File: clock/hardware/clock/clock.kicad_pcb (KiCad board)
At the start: 2 copper layers, 26 parts, among them J1 USB_B_Micro, J2 7SEG_DEBUG, J3 Conn_ARM_JTAG_SWD_10, U1 LM1117-3.3, U2 AS1115, U3 LTC-4727JS, U4 STM32L151C8TxA, Y1 32.768kHz

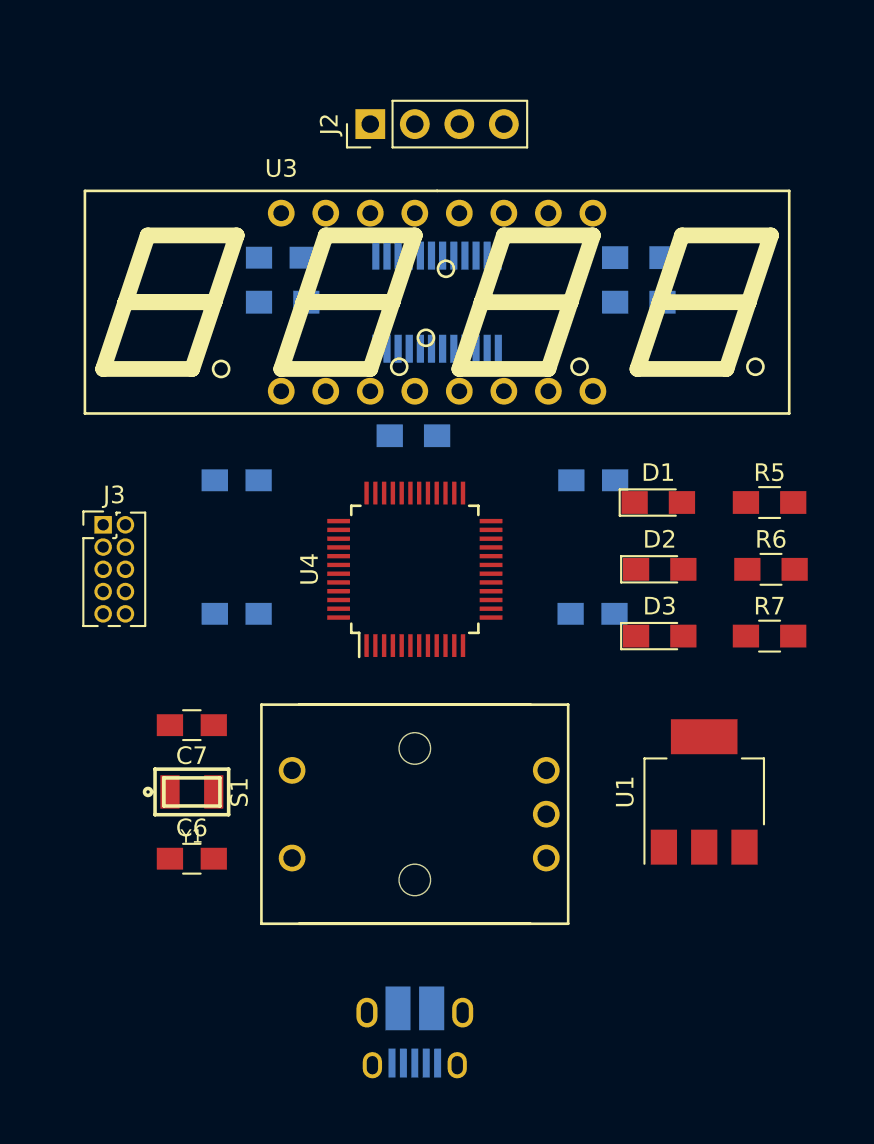
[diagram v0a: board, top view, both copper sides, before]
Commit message: Add clock edge cuts
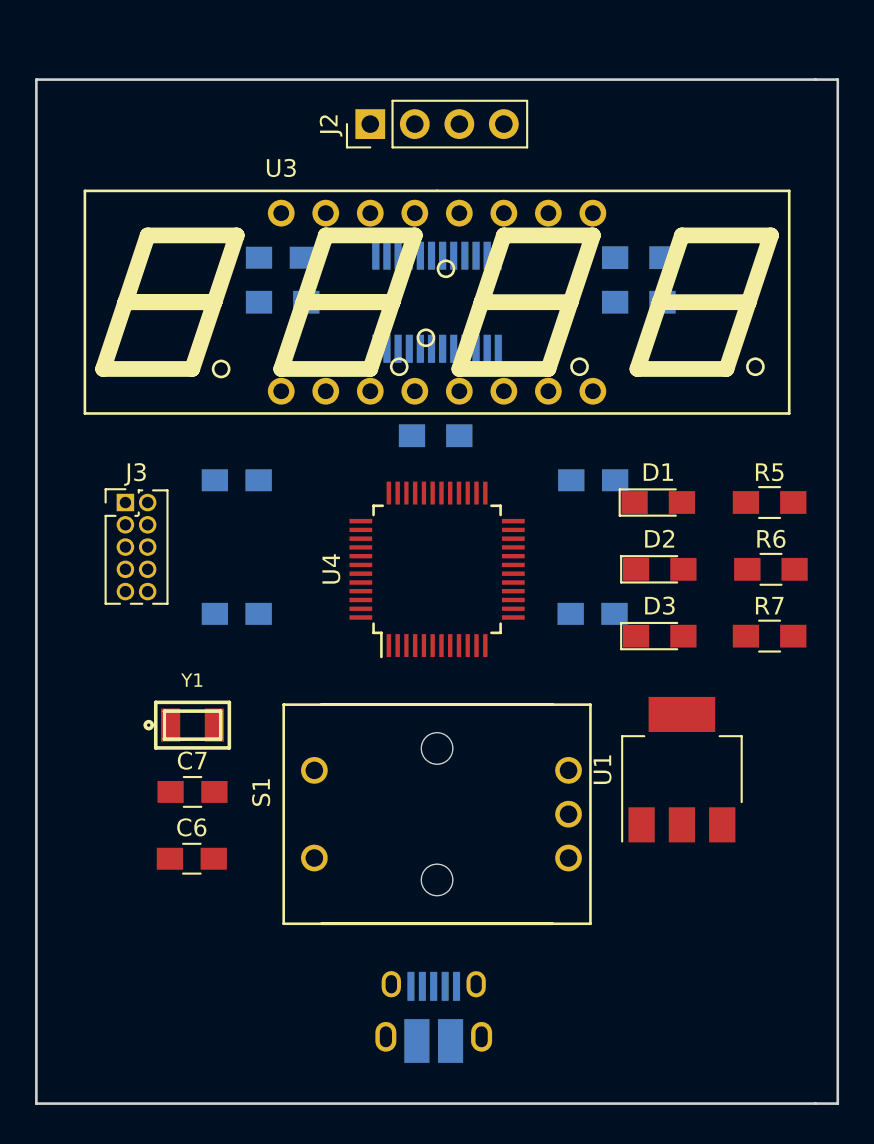
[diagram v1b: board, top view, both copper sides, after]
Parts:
- moved C7 3.81 mm to (69.9, 59.7), turned to 0 degrees
- moved Y1 3.81 mm to (69.9, 55.9)
- moved J3 1.80 mm to (66.0, 43.2)
- moved U1 1.80 mm to (97.8, 58.4)
- moved J1 1.75 mm to (83.6, 72.3), turned to 180 degrees
- moved R4 1.27 mm to (83.7, 39.4)
- moved S1 1.27 mm to (83.8, 61.0)
- moved U4 1.27 mm to (83.8, 47.0)
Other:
- board outline added: 45.7 x 58.4 mm
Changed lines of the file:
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@@
   (general
     (thickness 1.6)
-    (drawings 0)
+    (drawings 6)
     (tracks 0)
     (zones 0)
@@
   )
   (module Capacitors_SMD:C_0805_HandSoldering (layer F.Cu)
-    (at 69.83 55.88 180)
+    (at 69.87 59.69)
     (descr "Capacitor SMD 0805, hand soldering")
     (tags "capacitor 0805")
     (attr smd)
-    (fp_text reference C7 (at 0 -1.75 180) (layer F.SilkS)
-      (effects (font (size 1 1) (thickness 0.15)))
-    )
-    (fp_text value 10pf (at 0 1.75 180) (layer F.Fab)
-      (effects (font (size 1 1) (thickness 0.15)))
-    )
-    (fp_text user %R (at 0 -1.75 180) (layer F.Fab)
+    (fp_text reference C7 (at 0 -1.75) (layer F.SilkS)
+      (effects (font (size 1 1) (thickness 0.15)))
+    )
+    (fp_text value 10pf (at 0 1.75) (layer F.Fab)
+      (effects (font (size 1 1) (thickness 0.15)))
+    )
+    (fp_text user %R (at 0 -1.75) (layer F.Fab)
       (effects (font (size 1 1) (thickness 0.15)))
     )
@@
     (fp_line (start 2.25 0.87) (end 2.25 -0.88) (layer F.CrtYd) (width 0.05))
     (fp_line (start 2.25 0.87) (end -2.25 0.87) (layer F.CrtYd) (width 0.05))
-    (pad 1 smd rect (at -1.25 0 180) (size 1.5 1.25) (layers F.Cu F.Paste F.Mask)
+    (pad 1 smd rect (at -1.25 0) (size 1.5 1.25) (layers F.Cu F.Paste F.Mask)
       (net 4 "Net-(C7-Pad1)"))
-    (pad 2 smd rect (at 1.25 0 180) (size 1.5 1.25) (layers F.Cu F.Paste F.Mask)
+    (pad 2 smd rect (at 1.25 0) (size 1.5 1.25) (layers F.Cu F.Paste F.Mask)
       (net 2 GND))
     (model Capacitors_SMD.3dshapes/C_0805.wrl
@@
   )
   (module Connectors:USB_Micro-B_10103594-0001LF (layer B.Cu)
-    (at 82.55 73.66)
+    (at 83.63 72.28 180)
     (descr "Micro USB Type B 10103594-0001LF")
     (tags "USB USB_B USB_micro USB_OTG")
     (attr smd)
-    (fp_text reference J1 (at -1.5 4.62) (layer B.SilkS)
-      (effects (font (size 1 1) (thickness 0.15)) (justify mirror))
-    )
-    (fp_text value USB_B_Micro (at 0 -6.17) (layer B.Fab)
+    (fp_text reference J1 (at -6.35 1.27 180) (layer B.SilkS)
+      (effects (font (size 1 1) (thickness 0.15)) (justify mirror))
+    )
+    (fp_text value USB_B_Micro (at 0 4.97 180) (layer B.Fab)
       (effects (font (size 1 1) (thickness 0.15)) (justify mirror))
     )
@@
     (fp_line (start 4.25 3.4) (end 4.25 -4.45) (layer B.CrtYd) (width 0.05))
     (fp_line (start -4.25 3.4) (end 4.25 3.4) (layer B.CrtYd) (width 0.05))
-    (pad 6 smd rect (at 0.96 -1.62 270) (size 2.5 1.43) (layers B.Cu B.Paste B.Mask)
-      (net 2 GND))
-    (pad 6 smd rect (at -0.96 -1.62 270) (size 2.5 1.43) (layers B.Cu B.Paste B.Mask)
-      (net 2 GND))
-    (pad 6 thru_hole oval (at 2.73 -1.38 270) (size 1.7 1.2) (drill oval 1.2 0.7) (layers *.Cu *.Mask)
-      (net 2 GND))
-    (pad 6 thru_hole oval (at -2.73 -1.38 270) (size 1.7 1.2) (drill oval 1.2 0.7) (layers *.Cu *.Mask)
-      (net 2 GND))
-    (pad 6 thru_hole oval (at 2.42 1.62 270) (size 1.5 1.1) (drill oval 1.05 0.65) (layers *.Cu *.Mask)
-      (net 2 GND))
-    (pad 6 thru_hole oval (at -2.42 1.62 270) (size 1.5 1.1) (drill oval 1.05 0.65) (layers *.Cu *.Mask)
-      (net 2 GND))
-    (pad 5 smd rect (at 1.3 1.5 270) (size 1.65 0.4) (layers B.Cu B.Paste B.Mask)
-      (net 2 GND))
-    (pad 4 smd rect (at 0.65 1.5 270) (size 1.65 0.4) (layers B.Cu B.Paste B.Mask)
+    (pad 6 smd rect (at 0.96 -1.62 90) (size 2.5 1.43) (layers B.Cu B.Paste B.Mask)
+      (net 2 GND))
+    (pad 6 smd rect (at -0.96 -1.62 90) (size 2.5 1.43) (layers B.Cu B.Paste B.Mask)
+      (net 2 GND))
+    (pad 6 thru_hole oval (at 2.73 -1.38 90) (size 1.7 1.2) (drill oval 1.2 0.7) (layers *.Cu *.Mask)
+      (net 2 GND))
+    (pad 6 thru_hole oval (at -2.73 -1.38 90) (size 1.7 1.2) (drill oval 1.2 0.7) (layers *.Cu *.Mask)
+      (net 2 GND))
+    (pad 6 thru_hole oval (at 2.42 1.62 90) (size 1.5 1.1) (drill oval 1.05 0.65) (layers *.Cu *.Mask)
+      (net 2 GND))
+    (pad 6 thru_hole oval (at -2.42 1.62 90) (size 1.5 1.1) (drill oval 1.05 0.65) (layers *.Cu *.Mask)
+      (net 2 GND))
+    (pad 5 smd rect (at 1.3 1.5 90) (size 1.65 0.4) (layers B.Cu B.Paste B.Mask)
+      (net 2 GND))
+    (pad 4 smd rect (at 0.65 1.5 90) (size 1.65 0.4) (layers B.Cu B.Paste B.Mask)
       (net 10 "Net-(J1-Pad4)"))
-    (pad 3 smd rect (at 0 1.5 270) (size 1.65 0.4) (layers B.Cu B.Paste B.Mask)
+    (pad 3 smd rect (at 0 1.5 90) (size 1.65 0.4) (layers B.Cu B.Paste B.Mask)
       (net 11 "Net-(J1-Pad3)"))
-    (pad 2 smd rect (at -0.65 1.5 270) (size 1.65 0.4) (layers B.Cu B.Paste B.Mask)
+    (pad 2 smd rect (at -0.65 1.5 90) (size 1.65 0.4) (layers B.Cu B.Paste B.Mask)
       (net 12 "Net-(J1-Pad2)"))
-    (pad 1 smd rect (at -1.3 1.5 270) (size 1.65 0.4) (layers B.Cu B.Paste B.Mask)
+    (pad 1 smd rect (at -1.3 1.5 90) (size 1.65 0.4) (layers B.Cu B.Paste B.Mask)
       (net 13 "Net-(J1-Pad1)"))
   )
@@
   )
   (module Pin_Headers:Pin_Header_Straight_2x05_Pitch1.27mm (layer F.Cu)
-    (at 64.77 44.45)
+    (at 66.04 43.18)
     (descr "Through hole straight pin header, 2x05, 1.27mm pitch, double rows")
     (tags "Through hole pin header THT 2x05 1.27mm double row")
@@
   )
   (module Resistors_SMD:R_0805_HandSoldering (layer B.Cu)
-    (at 82.47 39.37)
+    (at 83.74 39.37)
     (descr "Resistor SMD 0805, hand soldering")
     (tags "resistor 0805")
@@
   )
   (module nome:PEC11 (layer F.Cu)
-    (at 82.55 60.96 90)
+    (at 83.82 60.96 90)
     (fp_text reference S1 (at 1.25 -10 90) (layer F.SilkS)
       (effects (font (size 1 1) (thickness 0.15)))
@@
   )
   (module TO_SOT_Packages_SMD:SOT-223 (layer F.Cu)
-    (at 99.06 59.69 90)
+    (at 97.79 58.42 90)
     (descr "module CMS SOT223 4 pins")
     (tags "CMS SOT")
@@
   )
   (module Housings_QFP:LQFP-48_7x7mm_Pitch0.5mm (layer F.Cu)
-    (at 82.55 46.99 90)
+    (at 83.82 46.99 90)
     (descr "48 LEAD LQFP 7x7mm (see MICREL LQFP7x7-48LD-PL-1.pdf)")
     (tags "QFP 0.5")
@@
   )
   (module crystal:ECS-31B_xtal (layer F.Cu)
-    (at 69.83 59.69)
+    (at 69.87 55.88)
     (descr http://www.ecsxtal.com/store/pdf/ecx-31b.pdf)
     (solder_paste_margin -0.0762)
     (attr smd)
-    (fp_text reference Y1 (at 0 2.54) (layer F.SilkS)
+    (fp_text reference Y1 (at 0 -2.54) (layer F.SilkS)
       (effects (font (size 0.762 0.762) (thickness 0.1524)))
     )
@@
     )
   )
+  (gr_line (start 106.68 19.05) (end 105.41 19.05) (layer Edge.Cuts) (width 0.15))
+  (gr_line (start 106.68 77.47) (end 106.68 19.05) (layer Edge.Cuts) (width 0.15))
+  (gr_line (start 105.41 77.47) (end 106.68 77.47) (layer Edge.Cuts) (width 0.15))
+  (gr_line (start 60.96 77.47) (end 105.41 77.47) (layer Edge.Cuts) (width 0.15))
+  (gr_line (start 60.96 19.05) (end 60.96 77.47) (layer Edge.Cuts) (width 0.15))
+  (gr_line (start 105.41 19.05) (end 60.96 19.05) (layer Edge.Cuts) (width 0.15))
 )

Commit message: Connect all clock nets
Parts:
- J1: moved to F.Cu
- moved C5 23.4 mm to (97.8, 34.3), turned to 180 degrees
- moved R1 23.4 mm to (97.9, 36.8), turned to 180 degrees
- moved R3 23.1 mm to (72.3, 33.0)
- moved R2 22.9 mm to (72.5, 30.5)
- moved R4 13.1 mm to (72.3, 45.7), turned to 180 degrees
- moved D3 5.08 mm to (96.5, 45.7), turned to 180 degrees
- moved R7 5.08 mm to (102.8, 45.7)
- moved C6 3.81 mm to (69.9, 59.7)
- moved C7 3.81 mm to (69.9, 63.5)
- moved D2 1.27 mm to (96.5, 48.3), turned to 180 degrees
- moved R6 1.27 mm to (102.9, 48.3)
- turned C1 to 180 degrees
- turned D1 to 180 degrees
- turned J1 to 0 degrees
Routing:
- net GND: track 0.00 -> 82.4 mm, vias 0 -> 8
- net +3V3: track 0.00 -> 52.8 mm, vias 0 -> 10
- net /ENC_BTN: track 0.00 -> 34.6 mm
- net Net-(U2-Pad7): track 0.00 -> 27.9 mm
- net Net-(U2-Pad23): track 0.00 -> 26.1 mm, vias 0 -> 1
- net Net-(J2-Pad3): track 0.00 -> 24.9 mm, vias 0 -> 2
- net Net-(C7-Pad1): track 0.00 -> 22.5 mm
- net Net-(J1-Pad1): track 0.00 -> 22.3 mm
- net Net-(U2-Pad22): track 0.00 -> 21.8 mm, vias 0 -> 2
- net Net-(J2-Pad2): track 0.00 -> 21.6 mm
- net Net-(C6-Pad1): track 0.00 -> 19.8 mm
- net Net-(U2-Pad3): track 0.00 -> 16.9 mm
- net /JTAG_TMS: track 0.00 -> 16.5 mm
- net Net-(U2-Pad2): track 0.00 -> 15.3 mm
- net /ENC_CW: track 0.00 -> 14.3 mm
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- added copper zone on F.Cu, net +3V3
- added copper zone on B.Cu, net GND

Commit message: Add clock logo
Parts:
- added G***: LOGO, LOGO, F.Cu at (69.8, 71.1)
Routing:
- net GND: track 82.4 -> 80.3 mm
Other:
- board text added: "by Blake"
- board text added: "picoclock"
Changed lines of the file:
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@@
   (general
     (thickness 1.6)
-    (drawings 6)
-    (tracks 280)
+    (drawings 8)
+    (tracks 279)
     (zones 0)
-    (modules 26)
+    (modules 27)
     (nets 79)
   )
@@
     (add_net "Net-(U4-Pad7)")
   )
+  (module LOGO (layer F.Cu)
+    (at 69.85 71.12)
+    (fp_text reference G*** (at 0 0) (layer F.SilkS) hide
+      (effects (font (size 1.524 1.524) (thickness 0.3)))
+    )
+    (fp_text value LOGO (at 0.75 0) (layer F.SilkS) hide
+      (effects (font (size 1.524 1.524) (thickness 0.3)))
+    )
+    (fp_poly (pts (xy 0.097259 -2.371475) (xy 0.174398 -2.333021) (xy 0.2413 -2.2733) (xy 0.34925 -2.16535)
+      (xy 0.34925 -0.145438) (xy 0.8255 0.334403) (xy 1.30175 0.814243) (xy 1.30175 0.965189)
+      (xy 1.276041 1.109236) (xy 1.206019 1.217078) (xy 1.102339 1.284301) (xy 0.975658 1.30649)
+      (xy 0.836631 1.27923) (xy 0.711201 1.209843) (xy 0.647238 1.155963) (xy 0.550749 1.066751)
+      (xy 0.430809 0.951374) (xy 0.296498 0.819001) (xy 0.156893 0.6788) (xy 0.021072 0.539939)
+      (xy -0.101887 0.411587) (xy -0.202906 0.302911) (xy -0.272908 0.22308) (xy -0.297231 0.191372)
+      (xy -0.311079 0.164395) (xy -0.322269 0.125261) (xy -0.331077 0.067547) (xy -0.337776 -0.015171)
+      (xy -0.342641 -0.129315) (xy -0.345947 -0.281309) (xy -0.347967 -0.477577) (xy -0.348977 -0.724542)
+      (xy -0.34925 -1.02624) (xy -0.34925 -2.16535) (xy -0.241301 -2.2733) (xy -0.158405 -2.344121)
+      (xy -0.079586 -2.375438) (xy -0.000001 -2.381251) (xy 0.097259 -2.371475)) (layer F.SilkS) (width 0.01))
+    (fp_poly (pts (xy 0.419504 -3.714108) (xy 0.901715 -3.627473) (xy 1.381246 -3.477497) (xy 1.507442 -3.427241)
+      (xy 1.814067 -3.274115) (xy 2.126253 -3.071523) (xy 2.430798 -2.83066) (xy 2.714499 -2.562725)
+      (xy 2.964156 -2.278915) (xy 3.12666 -2.053881) (xy 3.365695 -1.629518) (xy 3.54594 -1.185124)
+      (xy 3.667 -0.725607) (xy 3.728481 -0.255877) (xy 3.729989 0.219156) (xy 3.671131 0.694584)
+      (xy 3.551512 1.165498) (xy 3.414267 1.530005) (xy 3.222285 1.900189) (xy 2.976369 2.257076)
+      (xy 2.685966 2.591219) (xy 2.360524 2.893167) (xy 2.009492 3.153475) (xy 1.642318 3.362692)
+      (xy 1.530005 3.414267) (xy 1.062639 3.584394) (xy 0.589446 3.691724) (xy 0.106816 3.73679)
+      (xy -0.388862 3.720128) (xy -0.47625 3.711016) (xy -0.919583 3.628956) (xy -1.354594 3.487039)
+      (xy -1.773948 3.288898) (xy -2.170307 3.038169) (xy -2.536336 2.738487) (xy -2.639502 2.639212)
+      (xy -2.963186 2.272838) (xy -3.231732 1.877893) (xy -3.444318 1.458697) (xy -3.600125 1.01957)
+      (xy -3.698331 0.564831) (xy -3.738115 0.098801) (xy -3.734051 0) (xy -3.01625 0)
+      (xy -2.987448 0.444722) (xy -2.900866 0.863147) (xy -2.756239 1.255886) (xy -2.553305 1.623552)
+      (xy -2.291798 1.966756) (xy -2.068212 2.198009) (xy -1.736396 2.473543) (xy -1.382962 2.692246)
+      (xy -0.999755 2.858419) (xy -0.60325 2.970982) (xy -0.472605 2.990624) (xy -0.297678 3.004049)
+      (xy -0.097403 3.011059) (xy 0.109287 3.011453) (xy 0.303461 3.005033) (xy 0.466183 2.991598)
+      (xy 0.525981 2.982881) (xy 0.941443 2.877429) (xy 1.336681 2.713053) (xy 1.706729 2.492472)
+      (xy 2.046621 2.2184) (xy 2.198009 2.068211) (xy 2.361199 1.886676) (xy 2.489894 1.720817)
+      (xy 2.600162 1.547895) (xy 2.705976 1.349375) (xy 2.843113 1.038415) (xy 2.937441 0.73414)
+      (xy 2.993418 0.416893) (xy 3.015497 0.067015) (xy 3.01625 -0.019631) (xy 2.987703 -0.457162)
+      (xy 2.901525 -0.868732) (xy 2.756906 -1.256367) (xy 2.553035 -1.622096) (xy 2.289103 -1.967944)
+      (xy 2.198009 -2.068212) (xy 1.871958 -2.371857) (xy 1.521885 -2.616741) (xy 1.147177 -2.803128)
+      (xy 0.747222 -2.931281) (xy 0.321408 -3.001464) (xy 0 -3.01625) (xy -0.441493 -2.988827)
+      (xy -0.85357 -2.905662) (xy -1.239568 -2.765417) (xy -1.602825 -2.566752) (xy -1.946678 -2.308328)
+      (xy -2.091028 -2.176936) (xy -2.390607 -1.849347) (xy -2.631375 -1.497939) (xy -2.813656 -1.121955)
+      (xy -2.937771 -0.720639) (xy -3.004041 -0.293233) (xy -3.01625 0) (xy -3.734051 0)
+      (xy -3.718658 -0.3742) (xy -3.639138 -0.849852) (xy -3.498735 -1.323837) (xy -3.427241 -1.507443)
+      (xy -3.255365 -1.849213) (xy -3.030199 -2.186149) (xy -2.761742 -2.508252) (xy -2.459994 -2.805523)
+      (xy -2.134954 -3.067961) (xy -1.796621 -3.285569) (xy -1.507443 -3.427241) (xy -1.028861 -3.593968)
+      (xy -0.547219 -3.697356) (xy -0.063952 -3.737402) (xy 0.419504 -3.714108)) (layer F.SilkS) (width 0.01))
+  )
   (module Capacitors_SMD:C_0805_HandSoldering (layer B.Cu)
     (at 72.39 49.53 180)
@@
       (rotate (xyz 0 0 0))
     )
+  )
+  (gr_text "by Blake" (at 97.79 73.66) (layer F.SilkS)
+    (effects (font (size 0.75 0.75) (thickness 0.1875)))
+  )
+  (gr_text "picoclock\n" (at 97.79 71.12) (layer F.SilkS)
+    (effects (font (size 1.5 1.5) (thickness 0.3)))
   )
   (gr_line (start 106.68 19.05) (end 105.41 19.05) (layer Edge.Cuts) (width 0.15))
@@
   (via (at 90.17 59.69) (size 0.6858) (drill 0.3302) (layers F.Cu B.Cu) (net 2))
   (segment (start 91.32 60.96) (end 90.17 59.81) (width 0.1524) (layer F.Cu) (net 2))
-  (via (at 73.66 66.04) (size 0.6858) (drill 0.3302) (layers F.Cu B.Cu) (net 2))
-  (segment (start 75.478001 64.221999) (end 73.66 66.04) (width 0.1524) (layer F.Cu) (net 2))
-  (segment (start 76.058001 64.221999) (end 75.478001 64.221999) (width 0.1524) (layer F.Cu) (net 2))
-  (segment (start 76.82 63.46) (end 76.058001 64.221999) (width 0.1524) (layer F.Cu) (net 2))
   (segment (start 71.12 59.69) (end 71.12 63.5) (width 0.1524) (layer F.Cu) (net 2))
-  (segment (start 71.12 63.5) (end 73.66 66.04) (width 0.1524) (layer F.Cu) (net 2))
   (via (at 90.17 44.45) (size 0.6858) (drill 0.3302) (layers F.Cu B.Cu) (net 2))
   (segment (start 89.88 44.74) (end 90.17 44.45) (width 0.1524) (layer F.Cu) (net 2))
@@
   (segment (start 85.05 70.66) (end 84.93 70.78) (width 0.1524) (layer F.Cu) (net 2))
   (segment (start 86.05 70.66) (end 85.05 70.66) (width 0.1524) (layer F.Cu) (net 2))
+  (via (at 73.66 63.5) (size 0.6858) (drill 0.3302) (layers F.Cu B.Cu) (net 2))
+  (segment (start 71.12 63.5) (end 73.66 63.5) (width 0.1524) (layer F.Cu) (net 2))
+  (segment (start 73.7 63.46) (end 73.66 63.5) (width 0.1524) (layer F.Cu) (net 2))
+  (segment (start 76.82 63.46) (end 73.7 63.46) (width 0.1524) (layer F.Cu) (net 2))
   (segment (start 69.398601 54.701399) (end 68.62 55.48) (width 0.1524) (layer F.Cu) (net 3))
   (segment (start 79.395083 54.701399) (end 69.398601 54.701399) (width 0.1524) (layer F.Cu) (net 3))
@@
   (segment (start 86.57 53.71) (end 91.32 58.46) (width 0.1524) (layer F.Cu) (net 19))
   (segment (start 86.57 51.34) (end 86.57 53.71) (width 0.1524) (layer F.Cu) (net 19))
+  (segment (start 92.310601 52.940601) (end 89.11 49.74) (width 0.1524) (layer F.Cu) (net 20))
   (segment (start 92.310601 63.935489) (end 92.310601 52.940601) (width 0.1524) (layer F.Cu) (net 20))
-  (segment (start 76.82 58.46) (end 80.181482 58.46) (width 0.1524) (layer F.Cu) (net 20))
-  (segment (start 86.172083 64.450601) (end 91.795489 64.450601) (width 0.1524) (layer F.Cu) (net 20))
-  (segment (start 80.181482 58.46) (end 86.172083 64.450601) (width 0.1524) (layer F.Cu) (net 20))
+  (segment (start 89.11 49.74) (end 88.17 49.74) (width 0.1524) (layer F.Cu) (net 20))
   (segment (start 91.795489 64.450601) (end 92.310601 63.935489) (width 0.1524) (layer F.Cu) (net 20))
-  (segment (start 92.310601 52.940601) (end 89.11 49.74) (width 0.1524) (layer F.Cu) (net 20))
-  (segment (start 89.11 49.74) (end 88.17 49.74) (width 0.1524) (layer F.Cu) (net 20))
+  (segment (start 83.86 58.46) (end 89.850601 64.450601) (width 0.1524) (layer F.Cu) (net 20))
+  (segment (start 76.82 58.46) (end 83.86 58.46) (width 0.1524) (layer F.Cu) (net 20))
+  (segment (start 89.850601 64.450601) (end 91.795489 64.450601) (width 0.1524) (layer F.Cu) (net 20))
   (via (at 88.9 24.13) (size 0.6858) (drill 0.3302) (layers F.Cu B.Cu) (net 23))
   (segment (start 90.17 36.83) (end 91.160601 35.839399) (width 0.1524) (layer B.Cu) (net 23))
